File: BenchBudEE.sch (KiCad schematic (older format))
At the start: 0 parts

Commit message: LED Driver
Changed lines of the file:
@@
 LIBS:fe_v+
 LIBS:fe_v-
+LIBS:ap5726
 LIBS:BenchBudEE-cache
 EELAYER 27 0
@@
 F0 "LED_Driver" 89
 F1 "led_driver.sch" 89
-F2 "EN" I L 6300 4400 60
-F3 "FREQ" I L 6300 4550 60
-F4 "String+" O R 8050 4400 60
-F5 "String-" I R 8050 4550 60
+F2 "String+" O R 8050 4400 60
+F3 "String-" I R 8050 4550 60
+F4 "LED_EN_PWM" I L 6300 4450 60
 $EndSheet
 $Sheet

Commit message: Arduino
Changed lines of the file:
@@
 LIBS:fe_v-
 LIBS:ap5726
+LIBS:arduino_pins
 LIBS:BenchBudEE-cache
 EELAYER 27 0
@@
 Sheet 1 9
 Title ""
-Date "7 feb 2014"
+Date "8 feb 2014"
 Rev ""
 Comp ""
@@
 $EndDescr
 $Sheet
-S 1100 3250 2200 3600
+S 1100 3250 1650 3500
 U 52E63D44
 F0 "Arduino" 89
 F1 "arduino.sch" 89
-F2 "MOSI" O R 3300 5000 60
-F3 "MISO" I R 3300 5250 60
-F4 "SCLK" O R 3300 5500 60
-F5 "Relay+" O R 3300 6200 60
-F6 "Relay-" I R 3300 6500 60
-F7 "CS_N" O R 3300 5700 60
-F8 "LED_EN" O R 3300 4250 60
-F9 "LED_FREQ" O R 3300 4450 60
-F10 "FAN_EN" O R 3300 3600 60
-F11 "TACH_MEAS" I R 3300 3800 60
+F2 "MOSI" O R 2750 4200 60
+F3 "MISO" I R 2750 4400 60
+F4 "SCLK" O R 2750 4900 60
+F5 "FAN_EN" O R 2750 4000 60
+F6 "TACH_MEAS" I R 2750 5150 60
+F7 "CURR_MEAS" I R 2750 5400 60
+F8 "RELAY+" O R 2750 6500 60
+F9 "RELAY-" O R 2750 6700 60
+F10 "V+ADJ_MON" I R 2750 3450 60
+F11 "V-ADJ_MON" I R 2750 3650 60
+F12 "LED_EN_PWM" O R 2750 6200 60
+F13 "DAC_CS_N" O R 2750 4650 60
+F14 "ADC_CS_N" O R 2750 5650 60
 $EndSheet
 $Sheet
@@
 $EndSheet
 $Sheet
-S 6300 5100 1700 900
+S 6300 4200 1700 900
 U 52E652F6
 F0 "Thermocouple" 89
 F1 "thermocouple5.sch" 89
-F2 "TC IN +" I R 8000 5300 60
-F3 "TC IN -" I R 8000 5550 60
-F4 "MISO" O L 6300 5300 60
-F5 "MOSI" I L 6300 5500 60
-F6 "SCLK" I L 6300 5700 60
-F7 "CS_N" I L 6300 5900 60
+F2 "TC IN +" I R 8000 4400 60
+F3 "TC IN -" I R 8000 4650 60
+F4 "MISO" O L 6300 4600 60
+F5 "MOSI" I L 6300 4350 60
+F6 "SCLK" I L 6300 4800 60
+F7 "CS_N" I L 6300 5000 60
 $EndSheet
 $Sheet
@@
 F0 "Relay" 89
 F1 "relay.sch" 89
-F2 "DIN+" I L 6300 6600 60
-F3 "DIN-" O L 6300 6750 60
-F4 "RELAY+" I R 7950 6600 60
-F5 "RELAY-" O R 7950 6750 60
-F6 "NC" B R 7950 6500 60
-$EndSheet
-$Sheet
-S 6300 4250 1750 450
+F2 "RELAY_NC" B R 7950 6450 60
+F3 "RELAY_NO" B R 7950 6600 60
+F4 "RELAY_COM" B R 7950 6750 60
+F5 "RELAY+" I L 6300 6500 60
+F6 "RELAY-" O L 6300 6700 60
+$EndSheet
+$Sheet
+S 6350 5500 1750 450
 U 52E65386
 F0 "LED_Driver" 89
 F1 "led_driver.sch" 89
-F2 "String+" O R 8050 4400 60
-F3 "String-" I R 8050 4550 60
-F4 "LED_EN_PWM" I L 6300 4450 60
+F2 "LED_EN_PWM" I L 6350 5700 60
+F3 "LED_STRING+" O R 8100 5650 60
+F4 "LED_STRING-" O R 8100 5800 60
 $EndSheet
 $Sheet
@@
 F0 "Fan" 89
 F1 "fan.sch" 89
-F2 "Power+" O R 8000 2850 60
-F3 "Power-" I R 8000 3050 60
-F4 "Tach_out" O L 6300 3850 60
-F5 "Fan_in" I L 6300 2750 60
-F6 "Tach" I R 8000 3350 60
-F7 "Current Measure" O L 6300 3700 60
-F8 "MOSI" I L 6300 2950 60
-F9 "MISO" O L 6300 3100 60
-F10 "CS_N" I L 6300 3250 60
-F11 "SCLK" I L 6300 3400 60
-$EndSheet
-$Sheet
-S 8700 1300 900  5400
+F2 "MOSI" I L 6300 2950 60
+F3 "MISO" O L 6300 3100 60
+F4 "CS_N" I L 6300 3250 60
+F5 "SCLK" I L 6300 3400 60
+F6 "FAN_OUT+" O R 8000 2700 60
+F7 "TACH_MEAS" O L 6300 3650 60
+F8 "FAN_EN" I L 6300 2700 60
+F9 "TACH_IN" I R 8000 3700 60
+F10 "CURR_MEAS" O L 6300 3800 60
+F11 "FAN_OUT-" O R 8000 2900 60
+$EndSheet
+$Sheet
+S 8700 1300 750  5650
 U 52E653FA
 F0 "Terminal_Block" 89
 F1 "terminal_block.sch" 89
+F2 "V+_ADJ" I L 8700 1600 60
+F3 "V-_ADJ" I L 8700 1750 60
+F4 "FAN_OUT+" O L 8700 2700 60
+F5 "FAN_OUT-" O L 8700 2900 60
+F6 "TACH_IN" I L 8700 3700 60
+F7 "LED_STRING+" O L 8700 5650 60
+F8 "LED_STRING-" O L 8700 5800 60
+F9 "TC_IN+" I L 8700 4400 60
+F10 "TC_IN-" I L 8700 4650 60
+F11 "RELAY_NC" B L 8700 6450 60
+F12 "RELAY_NO" B L 8700 6600 60
+F13 "RELAY_COM" B L 8700 6750 60
 $EndSheet
 $Sheet
@@
 F9 "V-_CURR_MON" O L 3450 2250 60
 $EndSheet
+Wire Wire Line
+	5250 1600 8700 1600
+Wire Wire Line
+	5250 1750 8700 1750
+Wire Wire Line
+	8000 2700 8700 2700
+Wire Wire Line
+	8000 2900 8700 2900
+Wire Wire Line
+	8000 3700 8700 3700
+Wire Wire Line
+	7950 6450 8700 6450
+Wire Wire Line
+	7950 6600 8700 6600
+Wire Wire Line
+	7950 6750 8700 6750
+Wire Wire Line
+	2750 3450 2850 3450
+Wire Wire Line
+	2850 3450 2850 1800
+Wire Wire Line
+	2850 1800 3450 1800
+Wire Wire Line
+	2750 3650 2950 3650
+Wire Wire Line
+	2950 3650 2950 1950
+Wire Wire Line
+	2950 1950 3450 1950
+Wire Wire Line
+	2750 4000 3350 4000
+Wire Wire Line
+	3350 4000 3350 2700
+Wire Wire Line
+	3350 2700 6300 2700
+Wire Wire Line
+	2750 4200 4800 4200
+Wire Wire Line
+	3500 4200 3500 2950
+Wire Wire Line
+	3500 2950 6300 2950
+Wire Wire Line
+	2750 4400 4700 4400
+Wire Wire Line
+	3700 4400 3700 3100
+Wire Wire Line
+	3700 3100 6300 3100
+Wire Wire Line
+	2750 4650 3900 4650
+Wire Wire Line
+	3900 4650 3900 3250
+Wire Wire Line
+	3900 3250 6300 3250
+Wire Wire Line
+	2750 4900 4700 4900
+Wire Wire Line
+	4100 4900 4100 3400
+Wire Wire Line
+	4100 3400 6300 3400
+Wire Wire Line
+	2750 6500 6300 6500
+Wire Wire Line
+	2750 6700 6300 6700
+Wire Wire Line
+	8000 4400 8700 4400
+Wire Wire Line
+	8000 4650 8700 4650
+Wire Wire Line
+	8100 5650 8700 5650
+Wire Wire Line
+	8100 5800 8700 5800
+Wire Wire Line
+	2750 5150 4300 5150
+Wire Wire Line
+	4300 5150 4300 3650
+Wire Wire Line
+	4300 3650 6300 3650
+Wire Wire Line
+	2750 5400 4500 5400
+Wire Wire Line
+	4500 5400 4500 3800
+Wire Wire Line
+	4500 3800 6300 3800
+Wire Wire Line
+	2750 5650 4800 5650
+Wire Wire Line
+	4800 5650 4800 5000
+Wire Wire Line
+	4800 5000 6300 5000
+Wire Wire Line
+	4800 4200 4800 4350
+Wire Wire Line
+	4800 4350 6300 4350
+Connection ~ 3500 4200
+Wire Wire Line
+	4700 4400 4700 4600
+Wire Wire Line
+	4700 4600 6300 4600
+Connection ~ 3700 4400
+Wire Wire Line
+	4700 4900 4700 4800
+Wire Wire Line
+	4700 4800 6300 4800
+Connection ~ 4100 4900
 $EndSCHEMATC

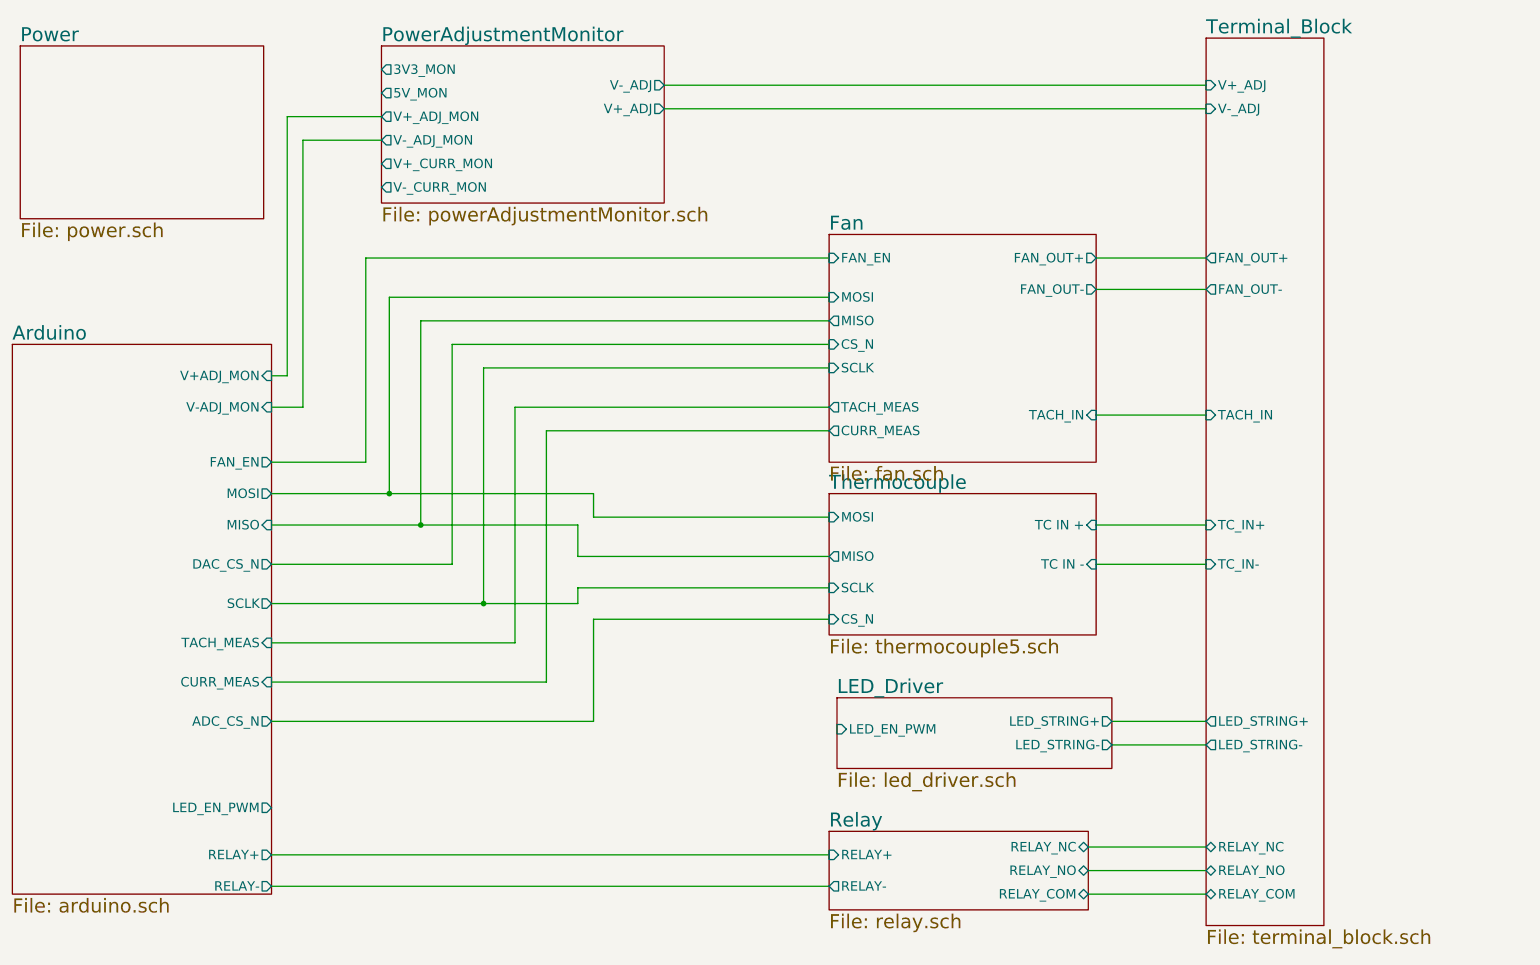
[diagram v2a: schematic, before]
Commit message: Fan/Power refactoring
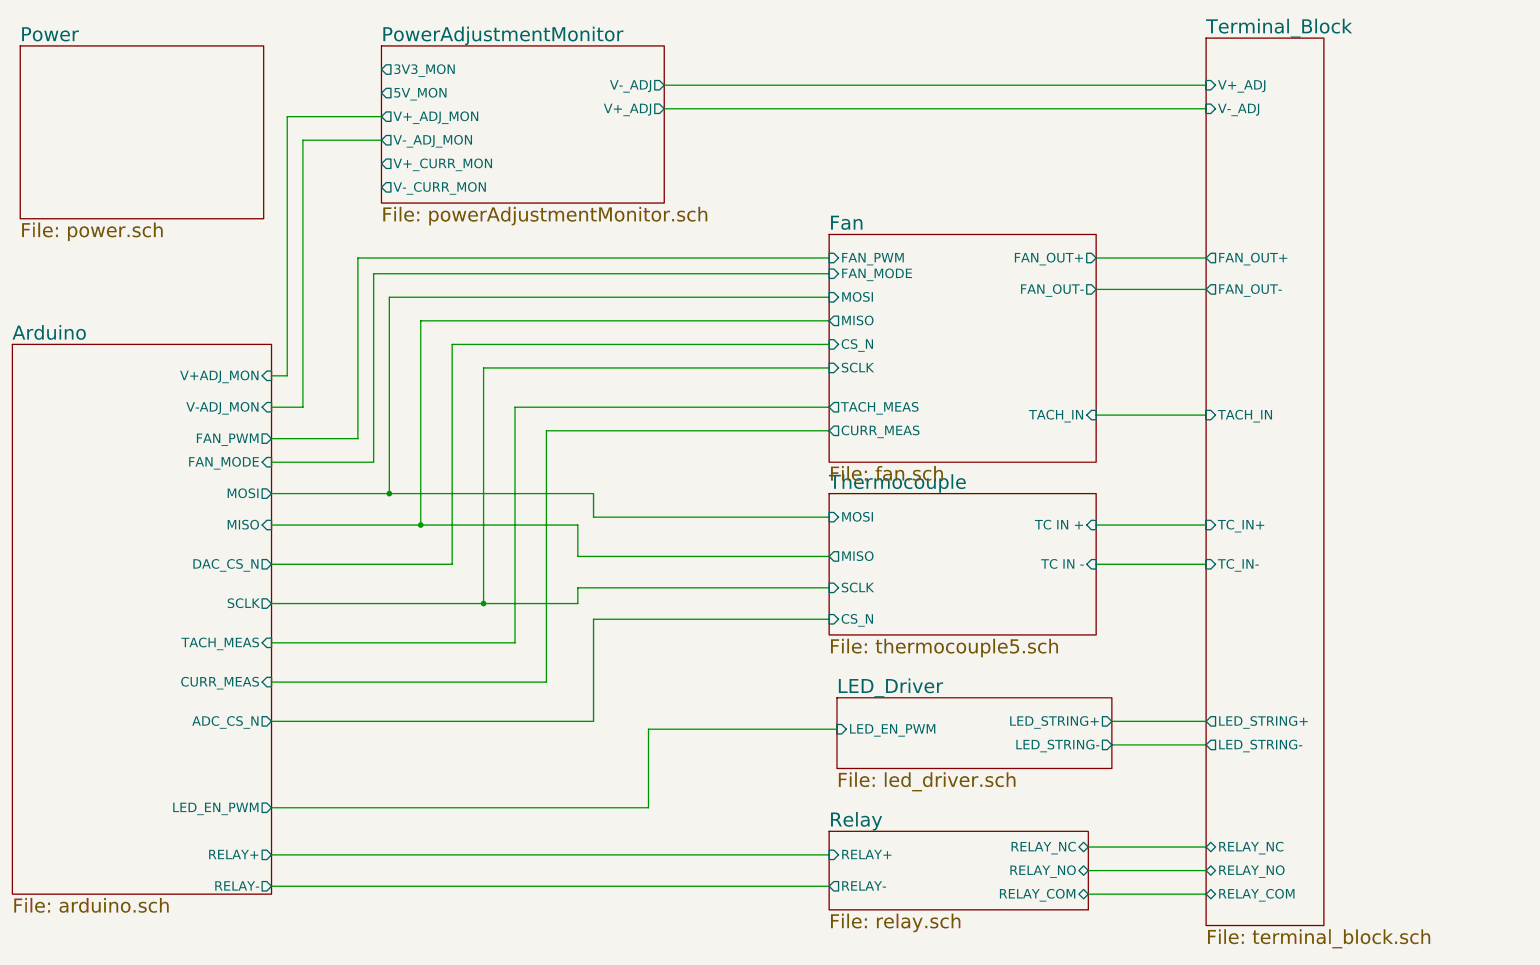
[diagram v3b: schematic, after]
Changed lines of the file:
@@
 F3 "MISO" I R 2750 4400 60
 F4 "SCLK" O R 2750 4900 60
-F5 "FAN_EN" O R 2750 4000 60
-F6 "TACH_MEAS" I R 2750 5150 60
-F7 "CURR_MEAS" I R 2750 5400 60
-F8 "RELAY+" O R 2750 6500 60
-F9 "RELAY-" O R 2750 6700 60
-F10 "V+ADJ_MON" I R 2750 3450 60
-F11 "V-ADJ_MON" I R 2750 3650 60
-F12 "LED_EN_PWM" O R 2750 6200 60
-F13 "DAC_CS_N" O R 2750 4650 60
-F14 "ADC_CS_N" O R 2750 5650 60
+F5 "TACH_MEAS" I R 2750 5150 60
+F6 "CURR_MEAS" I R 2750 5400 60
+F7 "RELAY+" O R 2750 6500 60
+F8 "RELAY-" O R 2750 6700 60
+F9 "V+ADJ_MON" I R 2750 3450 60
+F10 "V-ADJ_MON" I R 2750 3650 60
+F11 "LED_EN_PWM" O R 2750 6200 60
+F12 "DAC_CS_N" O R 2750 4650 60
+F13 "ADC_CS_N" O R 2750 5650 60
+F14 "FAN_PWM" O R 2750 3850 60
+F15 "FAN_MODE" I R 2750 4000 60
 $EndSheet
 $Sheet
@@
 F6 "FAN_OUT+" O R 8000 2700 60
 F7 "TACH_MEAS" O L 6300 3650 60
-F8 "FAN_EN" I L 6300 2700 60
-F9 "TACH_IN" I R 8000 3700 60
-F10 "CURR_MEAS" O L 6300 3800 60
-F11 "FAN_OUT-" O R 8000 2900 60
+F8 "TACH_IN" I R 8000 3700 60
+F9 "CURR_MEAS" O L 6300 3800 60
+F10 "FAN_OUT-" O R 8000 2900 60
+F11 "FAN_PWM" I L 6300 2700 60
+F12 "FAN_MODE" I L 6300 2800 60
 $EndSheet
 $Sheet
@@
 	2950 1950 3450 1950
 Wire Wire Line
-	2750 4000 3350 4000
-Wire Wire Line
-	3350 4000 3350 2700
-Wire Wire Line
-	3350 2700 6300 2700
+	3300 2700 6300 2700
 Wire Wire Line
 	2750 4200 4800 4200
@@
 	4700 4800 6300 4800
 Connection ~ 4100 4900
+Wire Wire Line
+	5150 6200 5150 5700
+Wire Wire Line
+	5150 5700 6350 5700
+Wire Wire Line
+	5150 6200 2750 6200
+Wire Wire Line
+	2750 3850 3300 3850
+Wire Wire Line
+	3300 3850 3300 2700
+Wire Wire Line
+	2750 4000 3400 4000
+Wire Wire Line
+	3400 4000 3400 2800
+Wire Wire Line
+	3400 2800 6300 2800
 $EndSCHEMATC
